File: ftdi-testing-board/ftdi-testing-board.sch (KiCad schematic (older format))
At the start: 9 parts

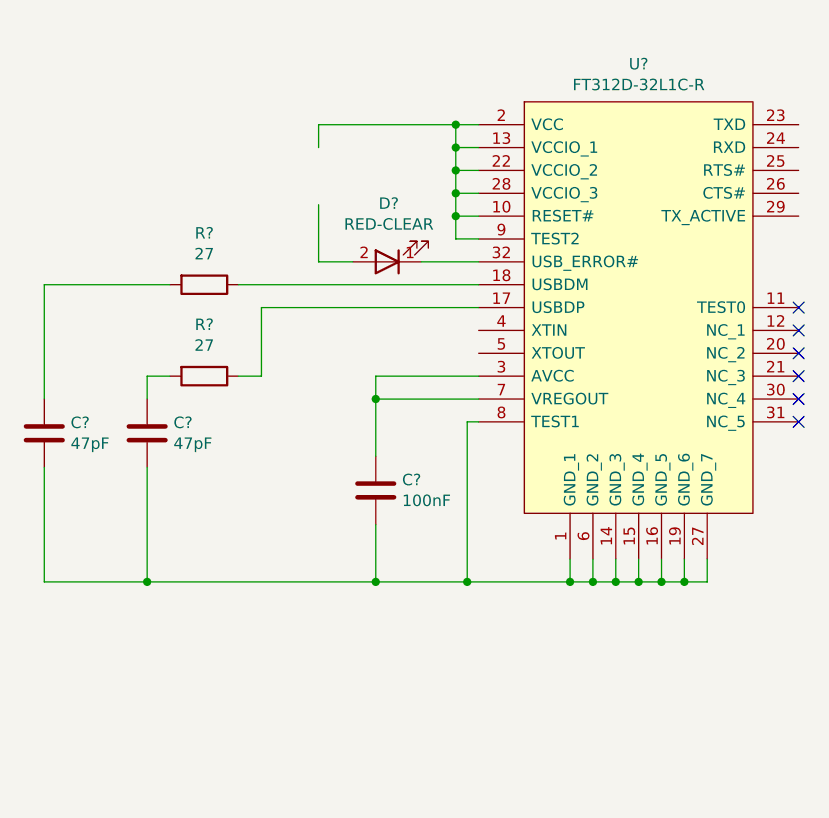
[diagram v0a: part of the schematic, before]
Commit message: Added capacitors to schematic
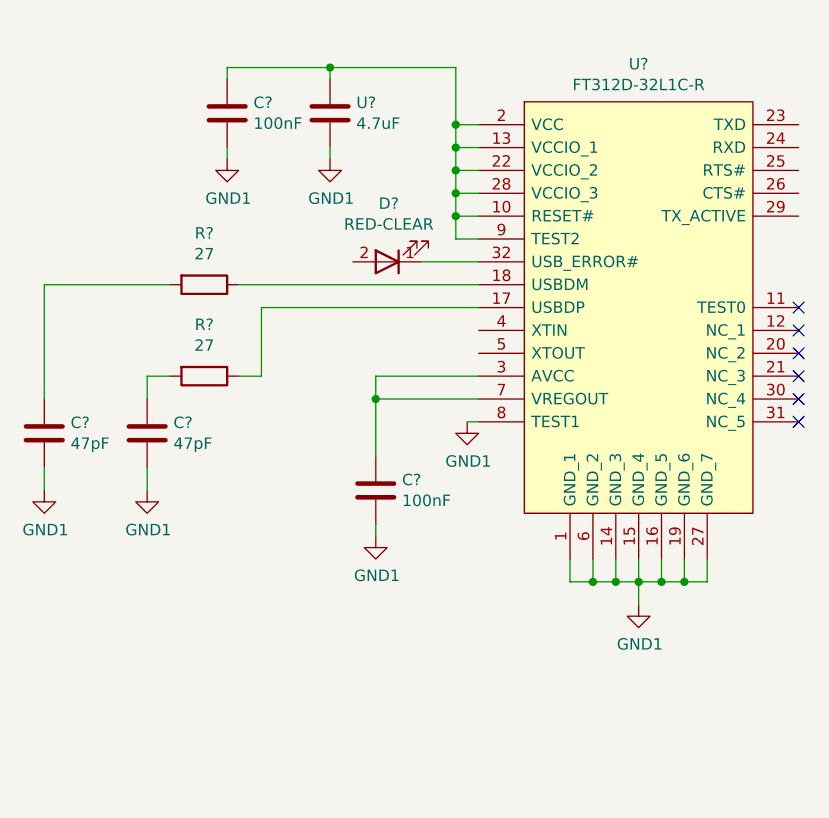
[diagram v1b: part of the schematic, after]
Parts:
- added C?: 100nF, Capacitor_SMD:C_0805_2012Metric, symbol C-100nF-0805:100nF
- added U?: 4.7uF, Capacitor_SMD:C_0805_2012Metric, symbol C-4.7uF-0805:4.7uF
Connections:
- net labels added: GND1
- wire segments 50 -> 49
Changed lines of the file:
@@
 	5100 1850 4850 1850
-Wire Wire Line
-	4550 1850 4400 1850
-Wire Wire Line
-	4400 1350 4400 1250
-Wire Wire Line
-	4400 1250 5000 1250
-Connection ~ 5000 1250
 Wire Wire Line
 	5100 1950 4050 1950
@@
 Connection ~ 5900 3250
 Wire Wire Line
-	5800 3250 5700 3250
-Wire Wire Line
 	5700 3250 5700 3150
 Connection ~ 5800 3250
@@
 	5500 3250 5500 3150
 Connection ~ 5600 3250
-Wire Wire Line
-	4400 1600 4400 1850
 $Comp
 L C-47pF-0805:47pF C?
@@
 	3200 1950 3750 1950
 Wire Wire Line
-	3650 2750 3650 3250
-Wire Wire Line
-	3650 3250 4650 3250
-Connection ~ 5500 3250
-Wire Wire Line
-	3200 2750 3200 3250
-Wire Wire Line
-	3200 3250 3650 3250
-Connection ~ 3650 3250
-Wire Wire Line
 	5100 2550 5050 2550
-Wire Wire Line
-	5050 2550 5050 3250
-Connection ~ 5050 3250
-Wire Wire Line
-	5050 3250 5500 3250
 $Comp
 L C-100nF-0805:100nF C?
@@
 	4650 2350 4650 2450
 Connection ~ 4650 2450
-Wire Wire Line
-	4650 3000 4650 3250
-Connection ~ 4650 3250
-Wire Wire Line
-	4650 3250 5050 3250
+$Comp
+L C-100nF-0805:100nF C?
+U 1 1 610EA512
+P 4000 1200
+F 0 "C?" H 4115 1246 50  0000 L CNN
+F 1 "100nF" H 4115 1155 50  0000 L CNN
+F 2 "Capacitor_SMD:C_0805_2012Metric" H 5200 1500 50  0001 C CNN
+F 3 "https://datasheets.avx.com/X7RDielectric.pdf" H 4000 1200 50  0001 C CNN
+F 4 "AVX Corporation" H 4800 1400 50  0001 C CNN "Manufacturer"
+F 5 "08055C104KAT2A" H 5600 1400 50  0001 C CNN "Manufacturer_Part_Number"
+F 6 "Digi-Key" H 4700 1300 50  0001 C CNN "Supplier 1"
+F 7 "478-1395-1-ND" H 5500 1300 50  0001 C CNN "Supplier Part Number 1"
+	1    4000 1200
+	1    0    0    -1
+$EndComp
+Wire Wire Line
+	4450 1050 4450 1000
+Wire Wire Line
+	4450 1000 5000 1000
+$Comp
+L C-4.7uF-0805:4.7uF U?
+U 1 1 610ECEC6
+P 4450 1200
+F 0 "U?" H 4565 1246 50  0000 L CNN
+F 1 "4.7uF" H 4565 1155 50  0000 L CNN
+F 2 "Capacitor_SMD:C_0805_2012Metric" H 5650 1400 50  0001 C CNN
+F 3 "http://www.samsungsem.com/kr/support/product-search/mlcc/CL21A475KQFNNNE.jsp" H 4450 1200 50  0001 C CNN
+F 4 "Samsung Electro-Mechanics" H 5450 1300 50  0001 C CNN "Manufacturer"
+F 5 "CL21A475KQFNNNE" H 6450 1300 50  0001 C CNN "Manufacturer_Part_Number"
+F 6 "Digi-Key" H 5150 1200 50  0001 C CNN "Supplier 1"
+F 7 "1276-1198-1-ND" H 5750 1200 50  0001 C CNN "Supplier Part Number 1"
+	1    4450 1200
+	1    0    0    -1
+$EndComp
+Wire Wire Line
+	4000 1050 4000 1000
+Wire Wire Line
+	4000 1000 4450 1000
+Connection ~ 4450 1000
+$Comp
+L power:GND1 #PWR?
+U 1 1 610F0A92
+P 3200 2850
+F 0 "#PWR?" H 3200 2600 50  0001 C CNN
+F 1 "GND1" H 3205 2677 50  0000 C CNN
+F 2 "" H 3200 2850 50  0001 C CNN
+F 3 "" H 3200 2850 50  0001 C CNN
+	1    3200 2850
+	1    0    0    -1
+$EndComp
+$Comp
+L power:GND1 #PWR?
+U 1 1 610F1704
+P 3650 2850
+F 0 "#PWR?" H 3650 2600 50  0001 C CNN
+F 1 "GND1" H 3655 2677 50  0000 C CNN
+F 2 "" H 3650 2850 50  0001 C CNN
+F 3 "" H 3650 2850 50  0001 C CNN
+	1    3650 2850
+	1    0    0    -1
+$EndComp
+$Comp
+L power:GND1 #PWR?
+U 1 1 610F1A26
+P 4650 3050
+F 0 "#PWR?" H 4650 2800 50  0001 C CNN
+F 1 "GND1" H 4655 2877 50  0000 C CNN
+F 2 "" H 4650 3050 50  0001 C CNN
+F 3 "" H 4650 3050 50  0001 C CNN
+	1    4650 3050
+	1    0    0    -1
+$EndComp
+$Comp
+L power:GND1 #PWR?
+U 1 1 610F2402
+P 5050 2550
+F 0 "#PWR?" H 5050 2300 50  0001 C CNN
+F 1 "GND1" H 5055 2377 50  0000 C CNN
+F 2 "" H 5050 2550 50  0001 C CNN
+F 3 "" H 5050 2550 50  0001 C CNN
+	1    5050 2550
+	1    0    0    -1
+$EndComp
+$Comp
+L power:GND1 #PWR?
+U 1 1 610F2945
+P 5800 3350
+F 0 "#PWR?" H 5800 3100 50  0001 C CNN
+F 1 "GND1" H 5805 3177 50  0000 C CNN
+F 2 "" H 5800 3350 50  0001 C CNN
+F 3 "" H 5800 3350 50  0001 C CNN
+	1    5800 3350
+	1    0    0    -1
+$EndComp
+$Comp
+L power:GND1 #PWR?
+U 1 1 610F4024
+P 4000 1400
+F 0 "#PWR?" H 4000 1150 50  0001 C CNN
+F 1 "GND1" H 4005 1227 50  0000 C CNN
+F 2 "" H 4000 1400 50  0001 C CNN
+F 3 "" H 4000 1400 50  0001 C CNN
+	1    4000 1400
+	1    0    0    -1
+$EndComp
+$Comp
+L power:GND1 #PWR?
+U 1 1 610F4B91
+P 4450 1400
+F 0 "#PWR?" H 4450 1150 50  0001 C CNN
+F 1 "GND1" H 4455 1227 50  0000 C CNN
+F 2 "" H 4450 1400 50  0001 C CNN
+F 3 "" H 4450 1400 50  0001 C CNN
+	1    4450 1400
+	1    0    0    -1
+$EndComp
+Wire Wire Line
+	5000 1000 5000 1250
+Connection ~ 5000 1250
+Wire Wire Line
+	4450 1350 4450 1400
+Wire Wire Line
+	4000 1350 4000 1400
+Wire Wire Line
+	3200 2750 3200 2850
+Wire Wire Line
+	3650 2750 3650 2850
+Wire Wire Line
+	4650 3000 4650 3050
+Wire Wire Line
+	5800 3250 5700 3250
+Wire Wire Line
+	5800 3350 5800 3250
 $EndSCHEMATC

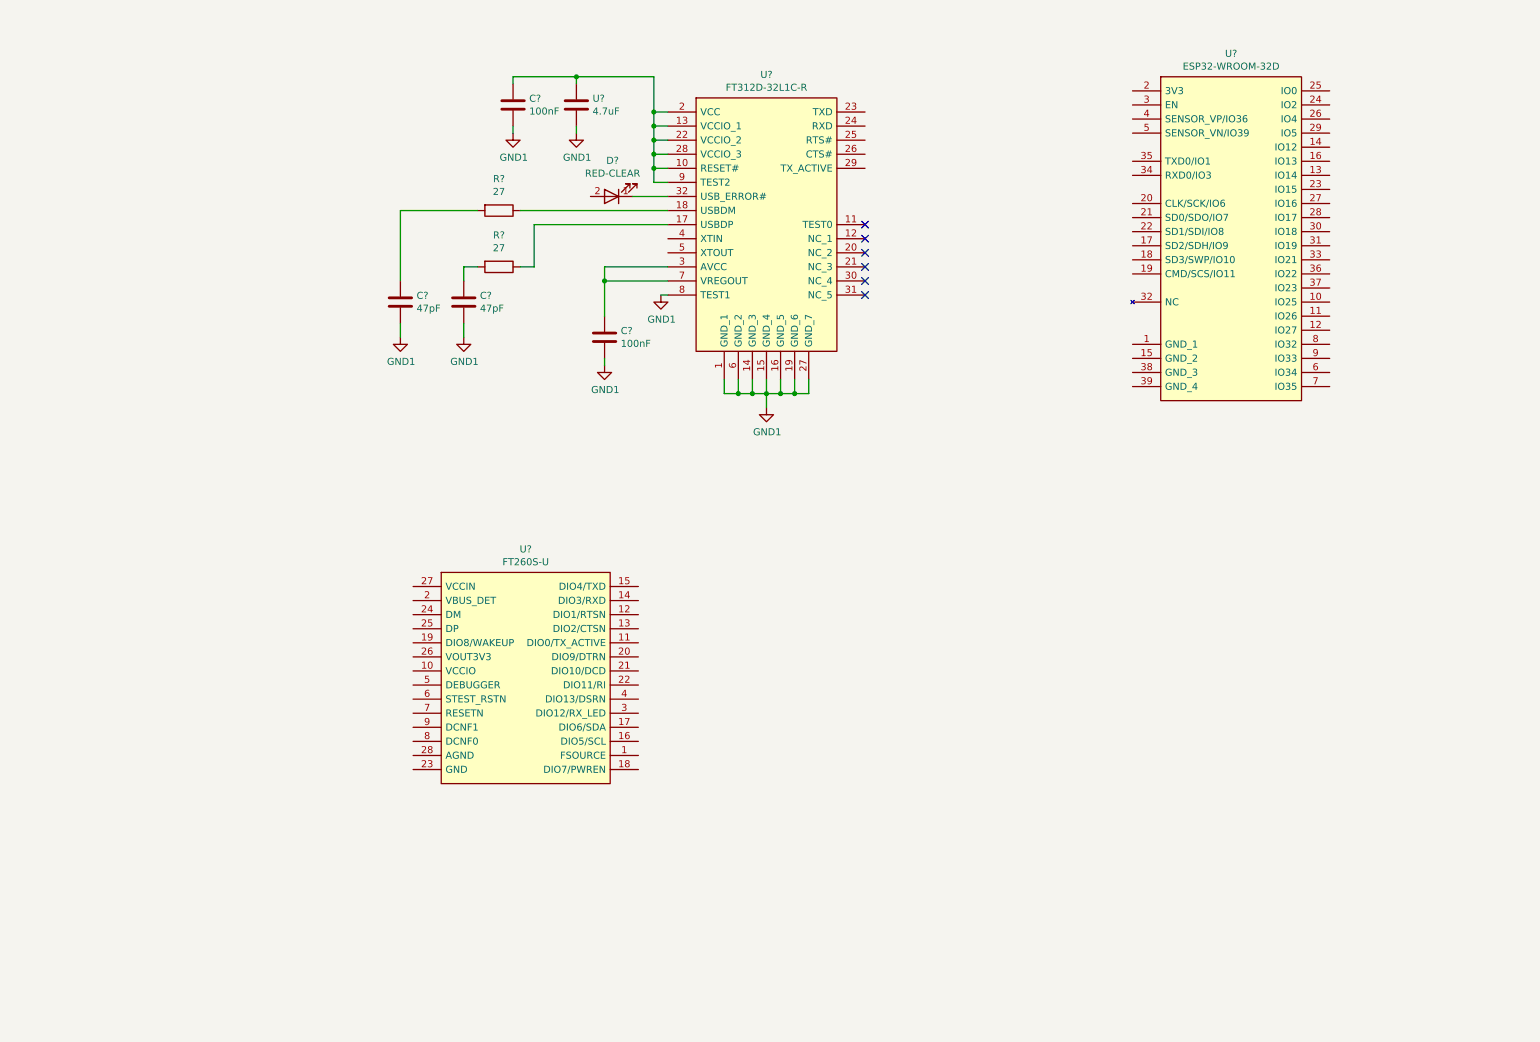
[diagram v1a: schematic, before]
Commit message: Added USB C, TVS and Ferrite Beads to Schematic
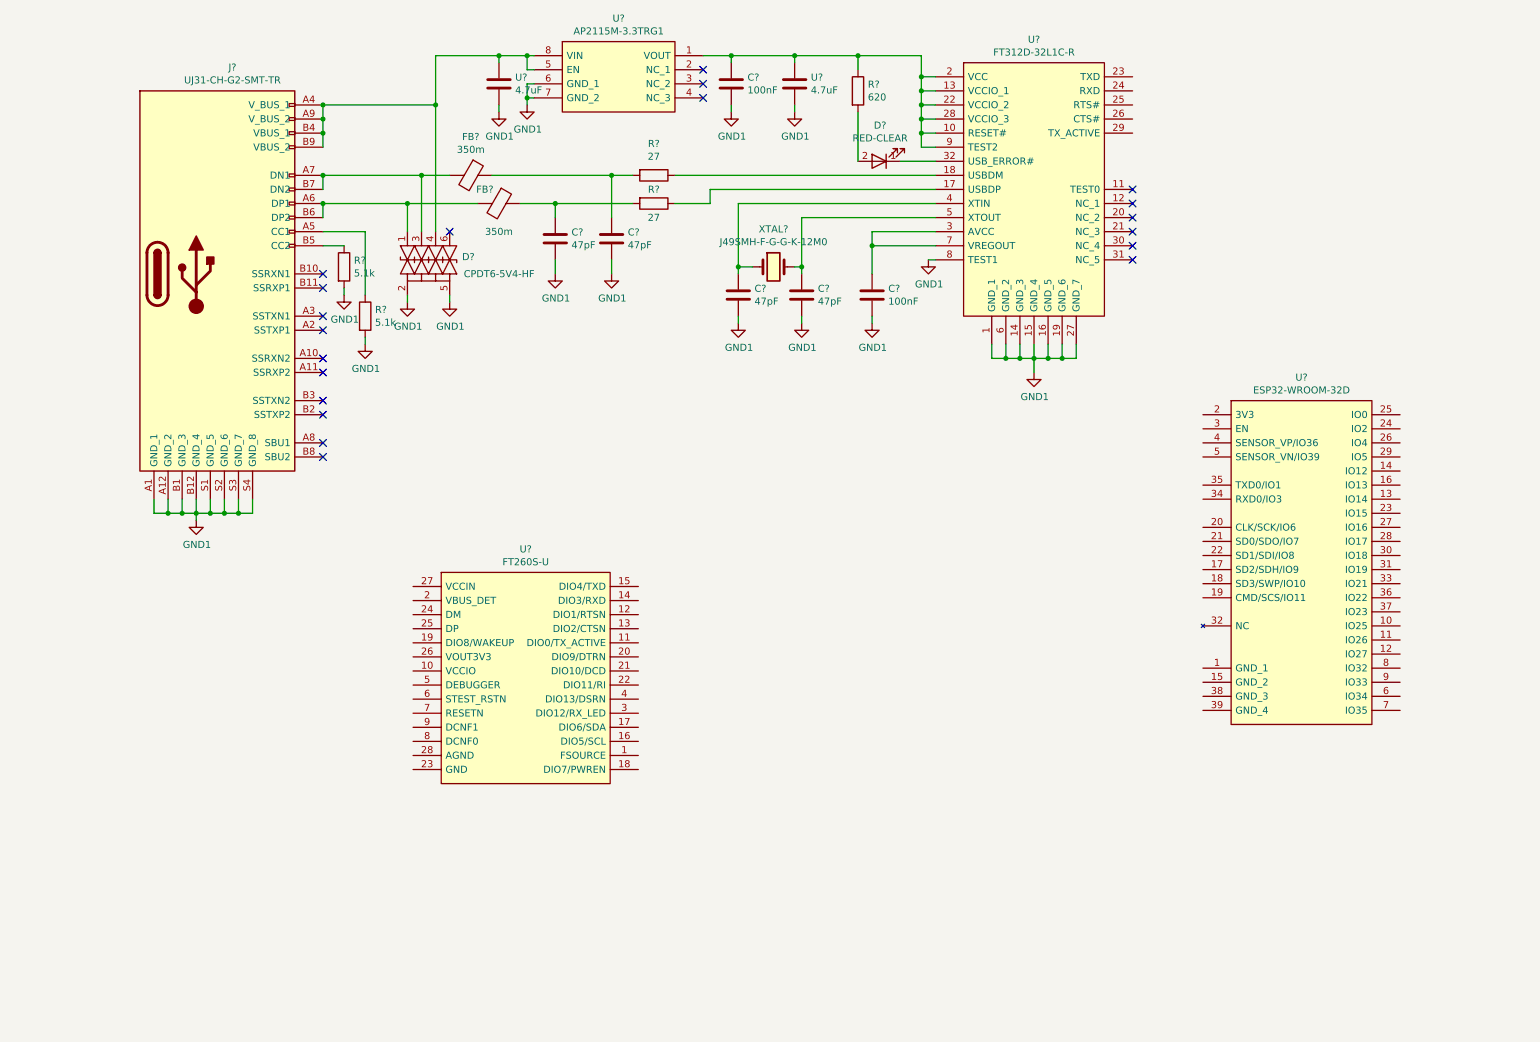
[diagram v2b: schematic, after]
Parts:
- added C? (x2): 47pF, Capacitor_SMD:C_0805_2012Metric, symbol C-47pF-0805:47pF
- added D?: CPDT6-5V4-HF, Package_TO_SOT_SMD:SOT-23-6_Handsoldering, symbol CPDT6-5V4-HF:CPDT6-5V4-HF
- added FB? (x2): 350m, Resistor_SMD:R_0805_2012Metric, symbol FB-350m-300mA-0805:350m
- added J?: UJ31-CH-G2-SMT-TR, UJ31CHG2SMTTR, symbol UJ31-CH-G2-SMT-TR:UJ31-CH-G2-SMT-TR
- added R?: 620, Resistor_SMD:R_0805_2012Metric, symbol R-620-0805:620
- added R? (x2): 5.1k, Resistor_SMD:R_0805_2012Metric, symbol R-5.1k-0805:5.1k
- added U?: AP2115M-3.3TRG1, SOIC127P600X175-8N, symbol AP2115M-3.3TRG1:AP2115M-3.3TRG1
- added U?: 4.7uF, Capacitor_SMD:C_0805_2012Metric, symbol C-4.7uF-0805:4.7uF
- added XTAL?: J49SMH-F-G-G-K-12M0, J49SMHPGGK8M0, symbol J49SMH-F-G-G-K-12M0:J49SMH-F-G-G-K-12M0
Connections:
- net GND1: now also C?.2, C?.2, D?.2, D?.5, J?.A1 (GND_1), J?.A12 (GND_2), J?.B1 (GND_3), J?.B12 (GND_4), J?.S1 (GND_5), J?.S2 (GND_6), J?.S3 (GND_7), J?.S4 (GND_8), R?.2, R?.2, U?.2, U?.6 (GND_1), U?.7 (GND_2)
- net at C?.1, U?.1, U?.10 (RESET#)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: now also R?.1, U?.1 (VOUT)
- net at U?.4 (XTIN): now also C?.1, XTAL?.1
- net at U?.5 (XTOUT): now also C?.1, XTAL?.2
- net at R?.2: now also C?.1, FB?.1; no longer C?.1 (x2)
- net at D?.2 (A): now also R?.2
- new net: D?.4, J?.A4 (V_BUS_1), J?.A9 (V_BUS_2), J?.B4 (VBUS_1), J?.B9 (VBUS_2), U?.1, U?.5 (EN), U?.8 (VIN)
- new net: J?.A5 (CC1), R?.1
- new net: D?.1, FB?.2, J?.A6 (DP1), J?.B6 (DP2)
- new net: D?.3, FB?.2, J?.A7 (DN1), J?.B7 (DN2)
- new net: J?.B5 (CC2), R?.1
- no-connect marks 6 -> 20
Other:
- moved on the sheet: C?, D?, R?, U?

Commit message: Added components for the FT312D, the FT260S and the auto reset circuit for the ESP
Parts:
- added C? (x2): 47pF, Capacitor_SMD:C_0805_2012Metric, symbol C-47pF-0805:47pF
- added C?: 100nF, Capacitor_SMD:C_0805_2012Metric, symbol C-100nF-0805:100nF
- added C? (x2): 1uF, Capacitor_SMD:C_0805_2012Metric, symbol C-1uF-0805:1uF
- added D? (x2): RED-CLEAR, LED_SMD:LED_0805_2012Metric, symbol LED-RED-CLEAR-0805:RED-CLEAR
- added J? (x3): Conn_01x04_Male, symbol Connector:Conn_01x04_Male
- added J? (x2): Conn_01x05_Male, symbol Connector:Conn_01x05_Male
- added J?: Conn_01x06_Male, symbol Connector:Conn_01x06_Male
- added Q? (x2): MMBT2222LT1G, Package_TO_SOT_SMD:SOT-23, symbol NPN-30V-600~mA:MMBT2222LT1G
- added R? (x2): 27, Resistor_SMD:R_0805_2012Metric, symbol R-27-0805:27
- added R? (x2): 620, Resistor_SMD:R_0805_2012Metric, symbol R-620-0805:620
- added R? (x4): 10K, Resistor_SMD:R_0805_2012Metric, symbol R-10K-0805:10K
- added U?: 4.7uF, Capacitor_SMD:C_0805_2012Metric, symbol C-4.7uF-0805:4.7uF
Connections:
- net labels added: ESP_IO0, ESP_RX, ESP_TX, GND, GND2, GND3
- wire segments 113 -> 227
- no-connect marks 20 -> 30
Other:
- note added: "3V3"
- note added: "5V"
- note added: "CTS"
- note added: "D+"
- note added: "D-"
- note added: "DTR"
- note added: "FT260S"
- note added: "FT312D"
- note added: "GND"
- note added: "RTS"
- note added: "RX"
- note added: "TX"
- note added: "USB-C 1"
- moved on the sheet: C?, D?, FB?, J?, R?, U?, XTAL?

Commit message: Finished schematic
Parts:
- added J1, J4: Conn_01x14_Male, Connector_PinSocket_2.54mm:PinSocket_1x14_P2.54mm_Vertical, symbol Connector:Conn_01x14_Male
- added J12, J8: Conn_01x05_Male, Connector_PinSocket_2.54mm:PinSocket_1x05_P2.54mm_Vertical, symbol Connector:Conn_01x05_Male
- added J5: Conn_01x10_Male, Connector_PinSocket_2.54mm:PinSocket_1x10_P2.54mm_Vertical, symbol Connector:Conn_01x10_Male
- added J6: Conn_01x08_Male, Connector_PinSocket_2.54mm:PinSocket_1x08_P2.54mm_Vertical, symbol Connector:Conn_01x08_Male
- added U1, U2: TS5A3153DCUR, Package_SO:VSSOP-8_2.3x2mm_P0.5mm, symbol TS5A3153DCUR:TS5A3153DCUR
- J10, J7, J9: renamed from J?; footprint (none) -> Connector_PinSocket_2.54mm:PinSocket_1x04_P2.54mm_Vertical
- J11, J13: renamed from J?; footprint (none) -> Connector_PinSocket_2.54mm:PinSocket_1x05_P2.54mm_Vertical
- J2: renamed from J?; footprint (none) -> Connector_PinSocket_2.54mm:PinSocket_1x16_P2.54mm_Vertical
- J3: renamed from J?; footprint UJ31CHG2SMTTR -> UJ31CHG2SMTTR:UJ31CHG2SMTTR
- U3: renamed from U?; footprint ESP32WROOM32D -> ESP32-WROOM-32D:ESP32-WROOM-32D
- U5: renamed from U?; footprint SOIC127P600X175-8N -> Package_SO:SOIC-8_3.9x4.9mm_P1.27mm
- U8: renamed from U?; footprint SOP65P640X120-28N -> Package_SO:TSSOP-28_4.4x9.7mm_P0.65mm
- U9: renamed from U?; footprint QFP80P900X900X160-32N -> Package_QFP:LQFP-32_7x7mm_P0.8mm
- XTAL1: renamed from XTAL?; footprint J49SMHPGGK8M0 -> Crystal:Crystal_SMD_HC49-SD_HandSoldering
- gave numbers to parts that had none: 35
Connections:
- net labels added: +3V3, CLK, CMD, ESP_EN, ESP_IO12, ESP_IO13, ESP_IO14, ESP_IO15, ESP_IO16, ESP_IO17, ESP_IO18, ESP_IO19, ESP_IO2, ESP_IO21, ESP_IO22, ESP_IO23, ESP_IO25, ESP_IO26, ESP_IO27, ESP_IO32, ESP_IO33, ESP_IO34, ESP_IO35, ESP_IO4, ESP_IO5, GNDA, SD0, SD1, SD2, SD3, SENSOR_VN, SENSOR_VP
- wire segments 227 -> 275
- no-connect marks 30 -> 27
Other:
- note added: "AUTO RESET"
- note added: "COM1"
- note added: "COM2"
- note added: "DCD"
- note added: "DSRN"
- note added: "DTRN"
- note added: "EN1"
- note added: "EN2"
- note added: "ESP32"
- note added: "IC SWITCH"
- note added: "IN1"
- note added: "IN2"
- note added: "NC1"
- note added: "NC2"
- note added: "NO1"
- note added: "NO2"
- note added: "RI"
- moved on the sheet: C1, C2, D4, J11, J2, R1, R13, R2, R5, R6, U3

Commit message: Changed footprint for header J2
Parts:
- J2: footprint Connector_PinSocket_2.54mm:PinSocket_1x16_P2.54mm_Vertical -> Connector_PinSocket_2.54mm:PinSocket_1x06_P2.54mm_Vertical
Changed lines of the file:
@@
 F 0 "J2" H 850 4600 50  0000 R CNN
 F 1 "Conn_01x06_Male" H 1200 4700 50  0000 R CNN
-F 2 "Connector_PinSocket_2.54mm:PinSocket_1x16_P2.54mm_Vertical" H 700 5150 50  0001 C CNN
+F 2 "Connector_PinSocket_2.54mm:PinSocket_1x06_P2.54mm_Vertical" H 700 5150 50  0001 C CNN
 F 3 "~" H 700 5150 50  0001 C CNN
 	1    700  5150
